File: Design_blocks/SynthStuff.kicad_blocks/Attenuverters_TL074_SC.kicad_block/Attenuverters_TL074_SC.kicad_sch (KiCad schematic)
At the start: 15 parts, among them U1 TL074

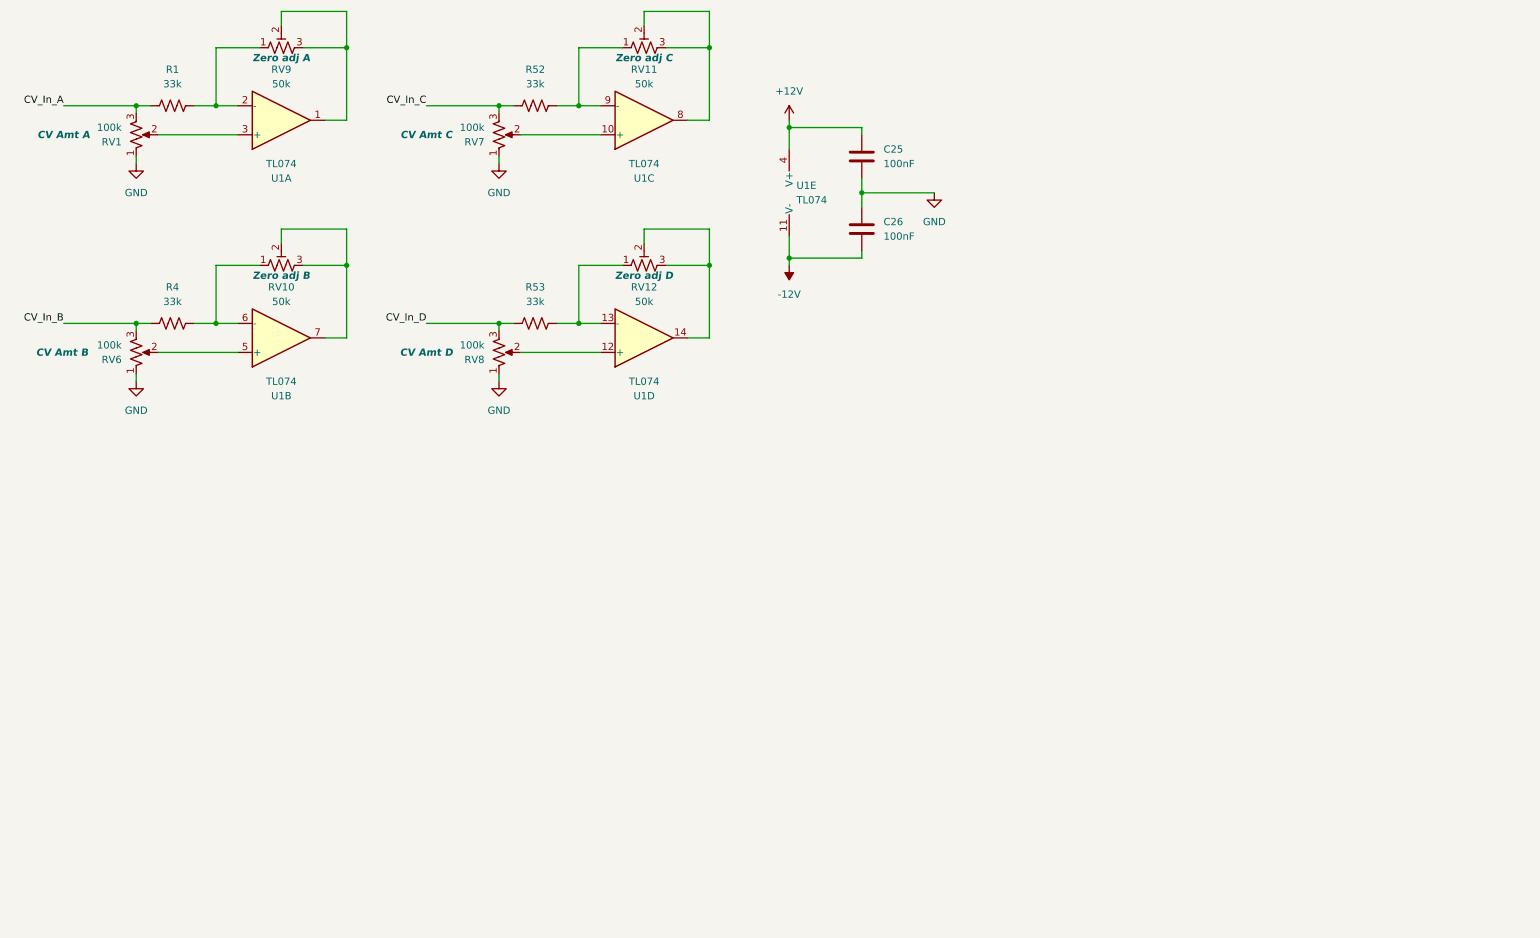
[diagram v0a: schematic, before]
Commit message: Added output label to attenuverter design blocks
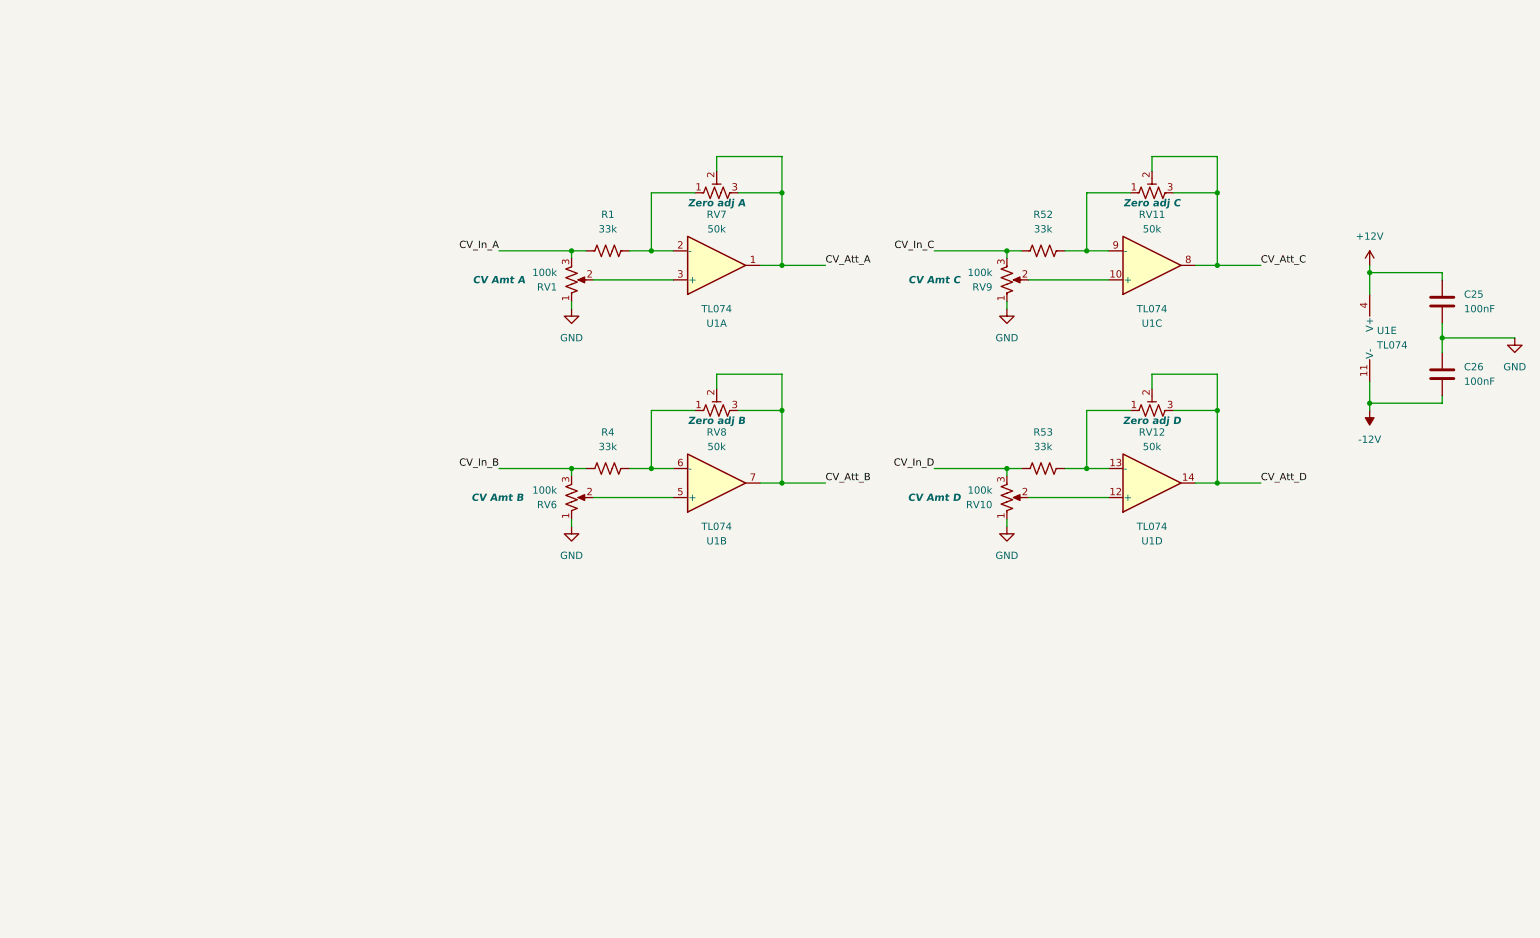
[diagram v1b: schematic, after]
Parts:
- renumbered RV8 to RV10, RV9 to RV7, RV10 to RV8, RV7 to RV9
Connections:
- net CV_Att_C: now reaches RV11.2, RV11.3, U1.8
- net CV_Att_A: now reaches RV7.2, RV7.3, U1.1
- net CV_Att_D: now reaches RV12.2, RV12.3, U1.14
- net CV_Att_B: now reaches RV8.2, RV8.3, U1.7
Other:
- moved on the sheet: C25, C26, R1, R4, R52, R53, RV1, RV10, RV11, RV12, RV6, RV7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

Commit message: Corrected attenuverter design block output labels
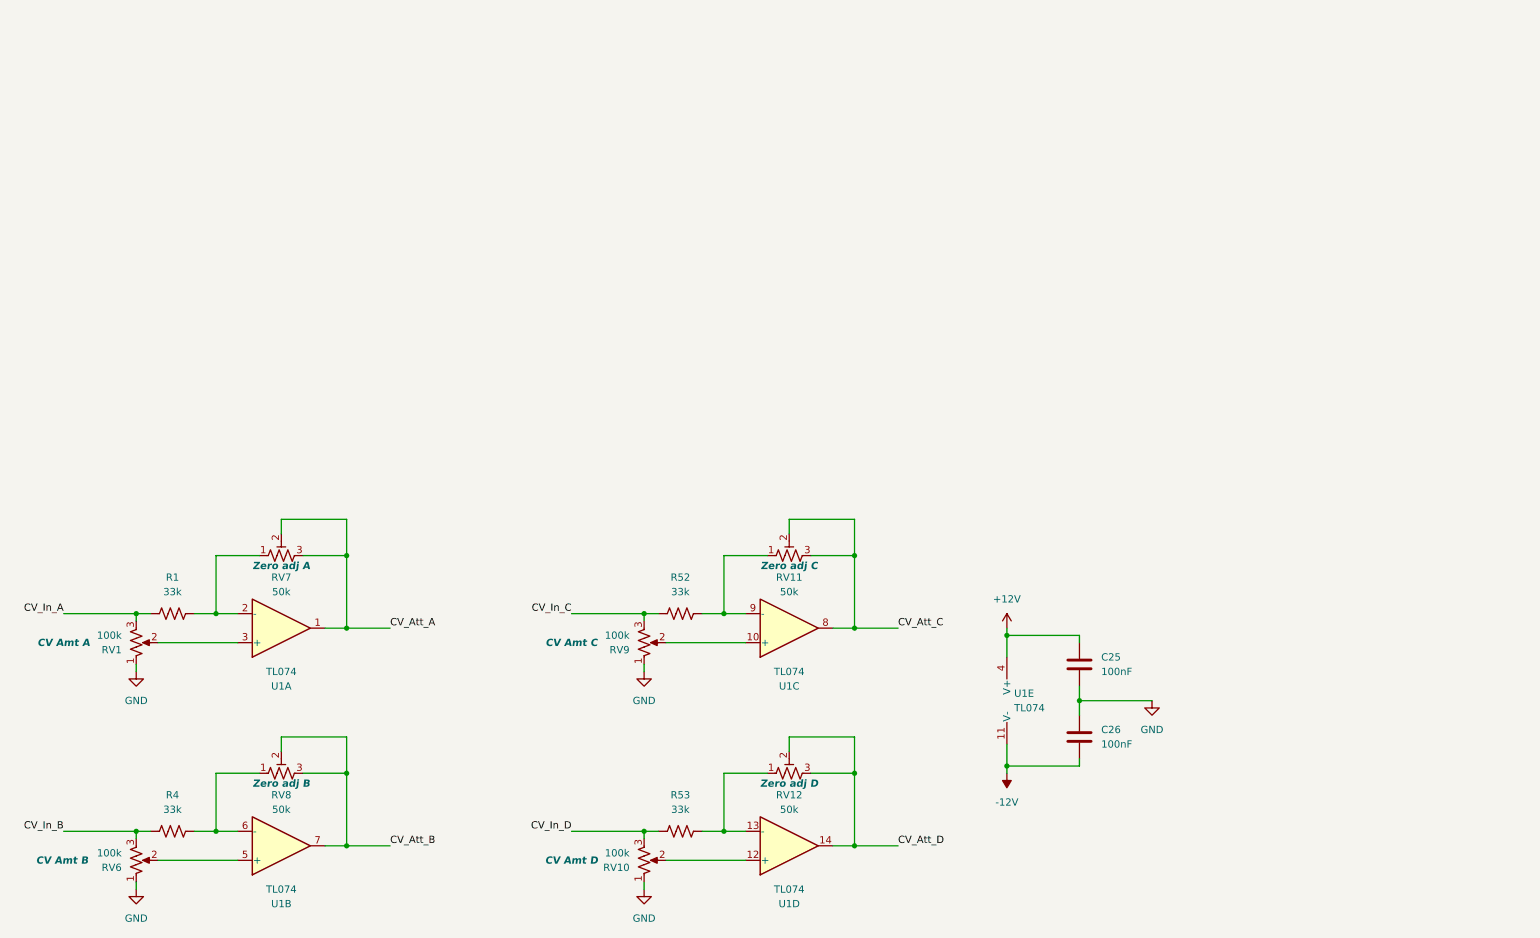
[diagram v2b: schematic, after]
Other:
- moved on the sheet: R1, RV1, RV10, RV12, RV7, RV9, U1A
